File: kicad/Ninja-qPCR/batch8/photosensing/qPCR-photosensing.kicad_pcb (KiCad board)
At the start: 2 copper layers, 86.8 x 88 mm, 63 parts, among them J1 Conn_01x14_Male, J2 Conn_01x02_Male, J3 Conn_01x04_Male, J4 Conn_01x04_Male, U1 ADS122C04IPWR, U10 MCP4551T-503E/MS, U11 PCA9955B, U13 SN74LV4051APWR, U14 CD74HC4067M96, U15 TS12A12511DCNR, U2 ADA2200ARUZ, U3 LMP7717MF_NOPB, U4 COM1305-0.032768-EXT-T-TR, U5 TS12A12511DCNR, U6 CD74HC4067M96, U7 SN74LVC1GU04DCKR, U8 LM7705MMX_NOPB, U9 SN74LVC1GU04DCKR

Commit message: change footprints
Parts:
- moved LEDN1 1.85 mm to (95.0, 51.2)
- moved LEDS1 1.85 mm to (95.0, 100.8)
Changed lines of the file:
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@@
   )
   (module Pin_Headers:Pin_Header_Straight_1x10_Pitch2.54mm (layer F.Cu)
-    (at 95 49.3005 90)
+    (at 95 51.1505 90)
     (descr "Through hole straight pin header, 1x10, 2.54mm pitch, single row")
     (tags "Through hole pin header THT 1x10 2.54mm single row")
@@
   )
   (module Pin_Headers:Pin_Header_Straight_1x10_Pitch2.54mm (layer F.Cu)
-    (at 95 102.6995 90)
+    (at 95 100.8495 90)
     (descr "Through hole straight pin header, 1x10, 2.54mm pitch, single row")
     (tags "Through hole pin header THT 1x10 2.54mm single row")

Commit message: change footprints
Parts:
- moved JPDS1 3.14 mm to (107.0, 88.1)
- moved JPDN1 2.86 mm to (107.0, 65.1)

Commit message: Photosensing artwork
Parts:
- moved R7 92.2 mm to (94.8, 109.6)
- moved U10 90.3 mm to (87.6, 104.3), turned to 180 degrees
- moved U11 87.5 mm to (88.5, 112.0), turned to 270 degrees
- moved C17 80.0 mm to (56.3, 118.5)
- moved C16 77.8 mm to (56.6, 113.3)
- moved TLID1 76.3 mm to (112.5, 92.9)
- moved TWELL1 75.8 mm to (112.5, 97.0)
- moved C14 72.5 mm to (88.7, 67.8), turned to 90 degrees
- moved C15 71.8 mm to (90.7, 66.8), turned to 90 degrees
- moved C11 69.1 mm to (87.2, 67.8), turned to 90 degrees
- moved FB1 69.0 mm to (92.4, 67.7), turned to 90 degrees
- moved J2 66.3 mm to (91.1, 93.1), turned to 270 degrees
- moved U8 64.9 mm to (84.3, 64.1)
- moved C12 64.4 mm to (91.0, 62.5), turned to 180 degrees
- moved C13 61.4 mm to (90.0, 60.6), turned to 180 degrees
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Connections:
- U13 pad 2: (no net) -> Net-(U13-Pad2)
- U13 pad 4: (no net) -> Net-(U13-Pad4)
- U14 pad 16: /Sheet60C04E5B/N_PD_OUT16 -> /Sheet60C04E5B/N_PD_OUT2
- U14 pad 17: /Sheet60C04E5B/N_PD_OUT15 -> /Sheet60C04E5B/N_PD_OUT4
- U14 pad 18: /Sheet60C04E5B/N_PD_OUT14 -> /Sheet60C04E5B/N_PD_OUT6
- U14 pad 19: /Sheet60C04E5B/N_PD_OUT13 -> /Sheet60C04E5B/N_PD_OUT8
- U14 pad 2: /Sheet60C04E5B/N_PD_OUT8 -> /Sheet60C04E5B/N_PD_OUT15
- U14 pad 20: /Sheet60C04E5B/N_PD_OUT12 -> /Sheet60C04E5B/N_PD_OUT10
- U14 pad 21: /Sheet60C04E5B/N_PD_OUT11 -> /Sheet60C04E5B/N_PD_OUT12
- U14 pad 22: /Sheet60C04E5B/N_PD_OUT10 -> /Sheet60C04E5B/N_PD_OUT14
- U14 pad 23: /Sheet60C04E5B/N_PD_OUT9 -> /Sheet60C04E5B/N_PD_OUT16
- U14 pad 3: /Sheet60C04E5B/N_PD_OUT7 -> /Sheet60C04E5B/N_PD_OUT13
- U14 pad 4: /Sheet60C04E5B/N_PD_OUT6 -> /Sheet60C04E5B/N_PD_OUT11
- U14 pad 5: /Sheet60C04E5B/N_PD_OUT5 -> /Sheet60C04E5B/N_PD_OUT9
- U14 pad 6: /Sheet60C04E5B/N_PD_OUT4 -> /Sheet60C04E5B/N_PD_OUT7
- U14 pad 7: /Sheet60C04E5B/N_PD_OUT3 -> /Sheet60C04E5B/N_PD_OUT5
- U14 pad 8: /Sheet60C04E5B/N_PD_OUT2 -> /Sheet60C04E5B/N_PD_OUT3
- U15 pad 5: (no net) -> Net-(U15-Pad5)
- U2 pad 2: (no net) -> Net-(U2-Pad2)
- U5 pad 5: (no net) -> Net-(U5-Pad5)
- U6 pad 16: /Sheet60AF0517/S_PD_OUT16 -> /Sheet60AF0517/S_PD_OUT15
- U6 pad 17: /Sheet60AF0517/S_PD_OUT15 -> /Sheet60AF0517/S_PD_OUT13
- U6 pad 18: /Sheet60AF0517/S_PD_OUT14 -> /Sheet60AF0517/S_PD_OUT11
- U6 pad 19: /Sheet60AF0517/S_PD_OUT13 -> /Sheet60AF0517/S_PD_OUT9
- U6 pad 2: /Sheet60AF0517/S_PD_OUT8 -> /Sheet60AF0517/S_PD_OUT2
- U6 pad 20: /Sheet60AF0517/S_PD_OUT12 -> /Sheet60AF0517/S_PD_OUT7
- U6 pad 21: /Sheet60AF0517/S_PD_OUT11 -> /Sheet60AF0517/S_PD_OUT5
- U6 pad 22: /Sheet60AF0517/S_PD_OUT10 -> /Sheet60AF0517/S_PD_OUT3
- U6 pad 23: /Sheet60AF0517/S_PD_OUT9 -> /Sheet60AF0517/S_PD_OUT1
- U6 pad 3: /Sheet60AF0517/S_PD_OUT7 -> /Sheet60AF0517/S_PD_OUT4
- U6 pad 5: /Sheet60AF0517/S_PD_OUT5 -> /Sheet60AF0517/S_PD_OUT8
- U6 pad 6: /Sheet60AF0517/S_PD_OUT4 -> /Sheet60AF0517/S_PD_OUT10
- U6 pad 7: /Sheet60AF0517/S_PD_OUT3 -> /Sheet60AF0517/S_PD_OUT12
- U6 pad 8: /Sheet60AF0517/S_PD_OUT2 -> /Sheet60AF0517/S_PD_OUT14
- U6 pad 9: /Sheet60AF0517/S_PD_OUT1 -> /Sheet60AF0517/S_PD_OUT16
- U7 pad 1: (no net) -> Net-(U7-Pad1)
- U9 pad 1: (no net) -> Net-(U9-Pad1)
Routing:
- net MUX_S0: track 0.00 -> 216.1 mm, vias 0 -> 4
- net MUX_S1: track 0.00 -> 211.1 mm, vias 0 -> 6
- net MUX_SELECT: track 0.00 -> 200.7 mm, vias 0 -> 6
- net 3V3D: track 0.00 -> 198.9 mm, vias 0 -> 7
- net MUX_S3: track 0.00 -> 189.6 mm, vias 0 -> 7
- net MUX_S2: track 0.00 -> 188.3 mm, vias 0 -> 6
- net GNDD: track 86.5 -> 243.6 mm, vias 0 -> 2
- net GNDA: track 0.00 -> 123.5 mm, vias 0 -> 2
- net N_LED_OUT8: track 0.00 -> 110.6 mm, vias 0 -> 1
- net N_LED_OUT7: track 0.00 -> 109.7 mm, vias 0 -> 1
- net N_LED_OUT6: track 0.00 -> 106.4 mm, vias 0 -> 1
- net N_LED_OUT5: track 0.00 -> 104.9 mm, vias 0 -> 1
- net N_LED_OUT4: track 0.00 -> 103.4 mm, vias 0 -> 1
- net N_LED_OUT3: track 0.00 -> 100.3 mm, vias 0 -> 1
- net N_LED_OUT2: track 0.00 -> 97.0 mm, vias 0 -> 1
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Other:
- outline, holes or cut-outs redrawn
- board text removed: "ADA2200"
- board text removed: "Gain Sw"
- board text removed: "LED Driver"
- board text removed: "Neg.V"
- board text removed: "North PD MUX"
- board text removed: "OpAmp"
- board text removed: "POT"
- board text removed: "Photo N/S Inverter"
- board text removed: "South PD MUX"

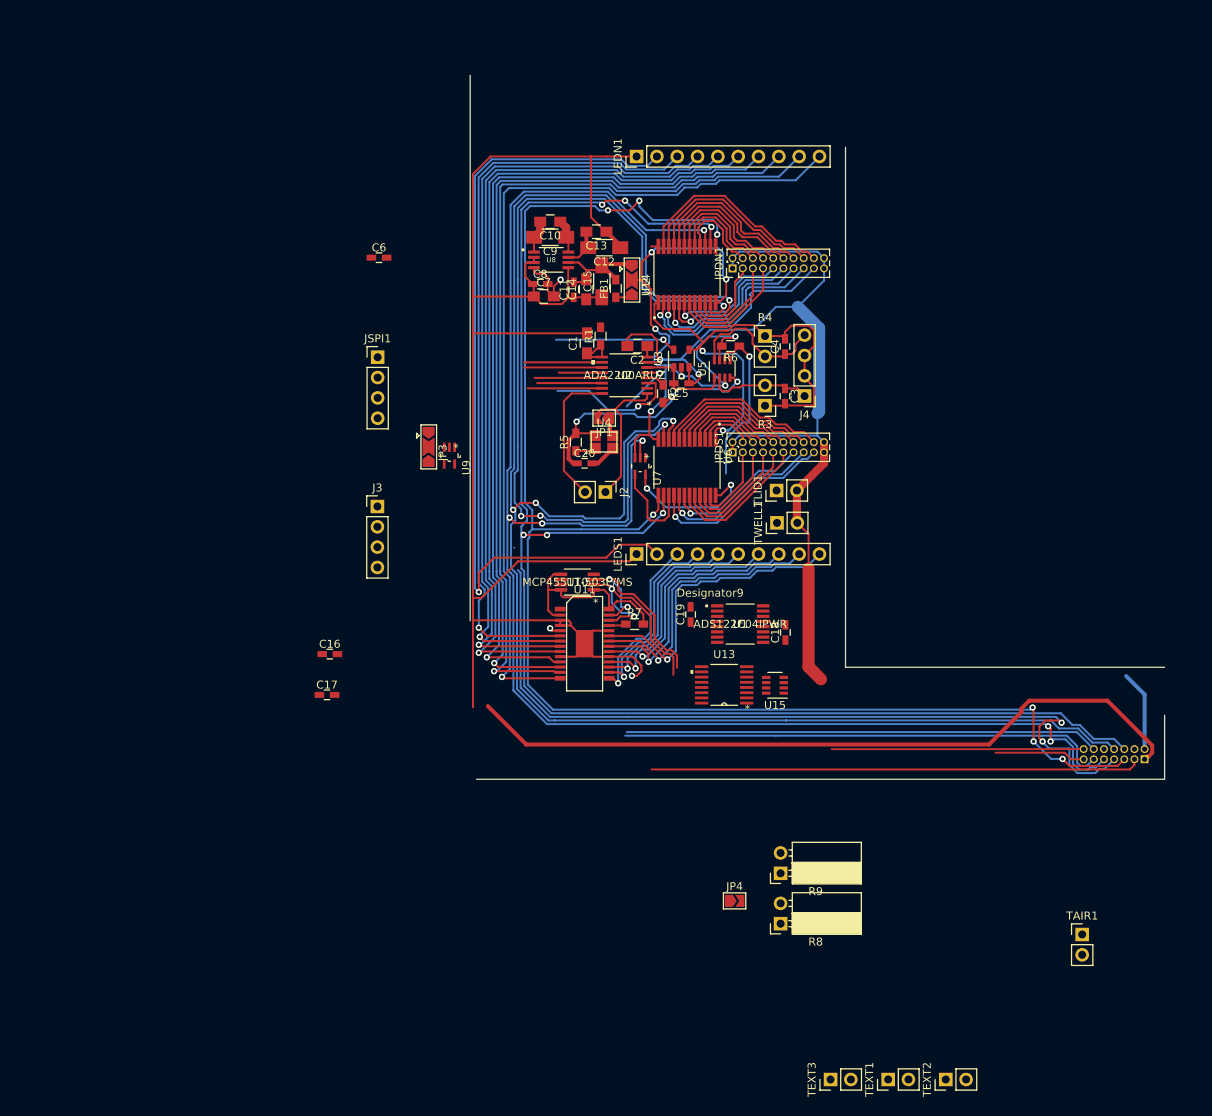
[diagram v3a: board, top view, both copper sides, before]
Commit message: Update photosensing board / replace thermistor connectors
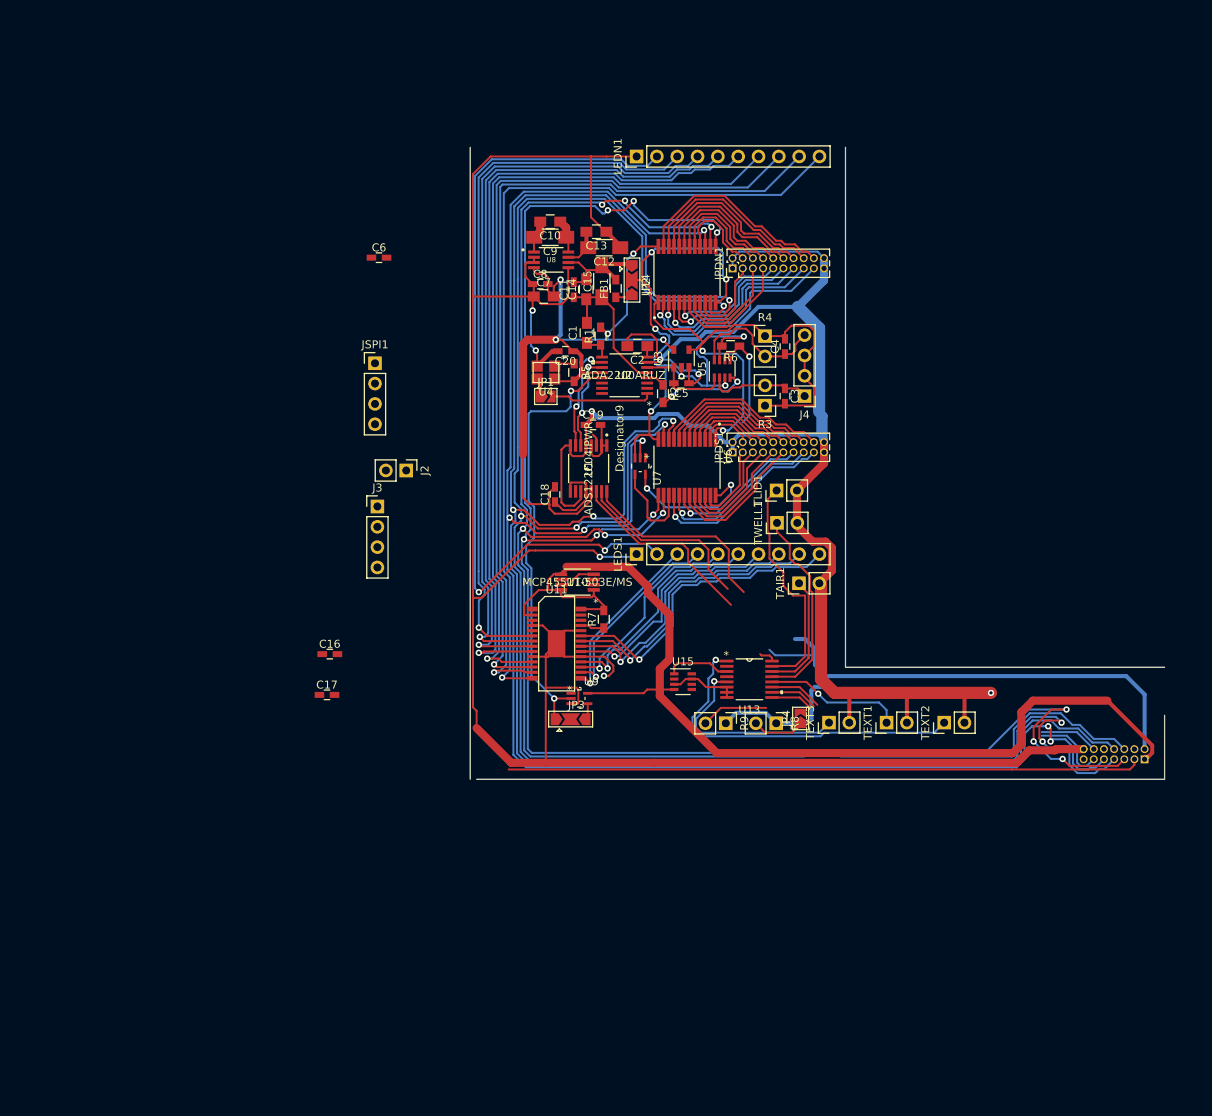
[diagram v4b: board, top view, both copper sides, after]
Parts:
- R8, R9: footprint Socket_Strips:Socket_Strip_Angled_1x02_Pitch2.54mm -> Pin_Headers:Pin_Header_Straight_1x02_Pitch2.54mm
- moved TAIR1 56.4 mm to (115.3, 104.5), turned to 90 degrees
- moved TEXT1 44.6 mm to (126.2, 121.9)
- moved TEXT2 44.6 mm to (133.4, 121.9)
- moved TEXT3 44.6 mm to (119.0, 121.9)
- moved JP3 38.4 mm to (86.8, 121.5), turned to 0 degrees
- moved U9 34.4 mm to (87.8, 118.9), turned to 0 degrees
- moved C18 33.6 mm to (84.8, 93.4)
- moved U1 27.2 mm to (89.0, 90.2), turned to 270 degrees
- moved C19 26.7 mm to (89.5, 84.7), turned to 0 degrees
- moved R8 25.1 mm to (112.5, 122.0), turned to 270 degrees
- moved J2 25.0 mm to (66.2, 90.4)
- moved JP4 24.2 mm to (115.5, 121.4), turned to 90 degrees
- moved R9 20.0 mm to (106.2, 122.0), turned to 270 degrees
- moved C20 14.2 mm to (86.1, 75.5), turned to 180 degrees
- moved U15 11.5 mm to (100.8, 116.8), turned to 0 degrees
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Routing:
- net GNDD: track 243.6 -> 327.2 mm, vias 2 -> 4
- net GNDA: track 123.5 -> 203.4 mm, vias 2 -> 4
- net 3V3A: track 10.1 -> 89.1 mm
- net 3V3D: track 198.9 -> 265.7 mm, vias 7 -> 9
- net I2C_SDA: track 85.1 -> 30.4 mm, vias 2 -> 0
- net I2C_SCL: track 87.9 -> 34.7 mm, vias 2 -> 0
- net PD_REF_PWM: track 8.46 -> 54.9 mm, vias 0 -> 2
- net THERM_EXT2: track 0.00 -> 43.9 mm, vias 0 -> 1
- net THERM_LID: track 0.00 -> 28.7 mm
- net THERM_EXT3: track 0.00 -> 25.9 mm, vias 0 -> 1
- net THERM_WELL: track 0.00 -> 25.2 mm
- net ADC_DRDY: track 0.00 -> 24.3 mm
- net MUX_S1: track 211.1 -> 232.1 mm
- net MUX_S3: track 189.6 -> 208.1 mm, vias 7 -> 9
- net XOUT: track 17.6 -> 0.00 mm
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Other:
- board size 86.8 x 88 mm -> 86.8 x 79 mm
- board text removed: "ADC"
- board text removed: "Ext Xtal"
- board text removed: "RCLK Inv"
- board text removed: "SPI Debug"

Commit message: minor changes
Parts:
- J1: value Conn_01x14_Male -> Conn_01x20_Male; footprint Pin_Headers:Pin_Header_Straight_2x07_Pitch1.27mm -> Pin_Headers:Pin_Header_Straight_2x10_Pitch1.27mm; moved to F.Cu
- moved J1 3.83 mm to (162.1, 125.2), turned to 270 degrees
- moved C1 0.20 mm to (88.6, 73.2)
- moved C10 0.20 mm to (84.0, 59.3)
- moved C11 0.20 mm to (87.0, 67.8)
- moved C12 0.20 mm to (90.8, 62.5)
- moved C13 0.20 mm to (89.8, 60.6)
- moved C14 0.20 mm to (88.5, 67.8)
- moved C15 0.20 mm to (90.5, 66.8)
- moved C18 0.20 mm to (84.6, 93.4)
- moved C19 0.20 mm to (89.3, 84.7)
- moved C3 0.20 mm to (113.3, 81.1)
- moved C4 0.20 mm to (113.3, 74.9)
- moved C7 0.20 mm to (83.2, 68.7)
- moved C8 0.20 mm to (82.8, 67.1)
- moved C9 0.20 mm to (84.0, 61.2)
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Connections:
- J1 pad 1: 3V3D -> (no net)
- J1 pad 10: ADC_DRDY -> VCC_LED
- J1 pad 11: I2C_SCL -> MUX_S2
- J1 pad 12: I2C_SDA -> MUX_S3
- J1 pad 13: THERM_R_SWITCH -> MUX_S0
- J1 pad 14: GNDD -> MUX_S1
- J1 pad 2: 3V3A -> (no net)
- J1 pad 3: VCC_LED -> (no net)
- J1 pad 4: AMP_GAIN_SW -> (no net)
- J1 pad 5: MUX_S3 -> (no net)
- J1 pad 6: MUX_S2 -> (no net)
- J1 pad 7: MUX_S1 -> 3V3A
- J1 pad 8: MUX_S0 -> 3V3D
- J1 pad 9: MUX_SELECT -> AMP_GAIN_SW
- U13 pad 2: Net-(U13-Pad2) -> (no net)
- U13 pad 4: Net-(U13-Pad4) -> (no net)
- U15 pad 5: Net-(U15-Pad5) -> (no net)
- U2 pad 2: Net-(U2-Pad2) -> (no net)
- U5 pad 5: Net-(U5-Pad5) -> (no net)
- U7 pad 1: Net-(U7-Pad1) -> (no net)
- U9 pad 1: Net-(U9-Pad1) -> (no net)
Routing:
- net 3V3D: track 265.7 -> 264.0 mm
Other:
- board size 86.8 x 79 mm -> 89.5 x 80.5 mm

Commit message: Photosensing artwork
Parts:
- removed the J1 at (162.1, 125.2)
- removed J2: Conn_01x02_Male, Pin_Headers:Pin_Header_Straight_1x02_Pitch2.54mm
- added J1: Conn_01x14_Male, Pin_Headers:Pin_Header_Straight_2x07_Pitch1.27mm, B.Cu at (158.5, 126.5)
- added J1: Conn_01x20_Male, Pin_Headers:Pin_Header_Straight_2x10_Pitch1.27mm, F.Cu at (158.4, 130.8)
- moved JSPI1 52.6 mm to (110.2, 55.8), turned to 90 degrees
- moved C16 37.2 mm to (92.6, 122.2), turned to 180 degrees
- moved TEXT2 30.9 mm to (105.2, 109.0), turned to 180 degrees
- moved J3 23.3 mm to (83.2, 84.5)
- moved C6 22.3 mm to (83.5, 71.6), turned to 90 degrees
- moved TEXT1 21.2 mm to (109.2, 109.0), turned to 180 degrees
- moved C17 20.7 mm to (76.6, 121.0), turned to 270 degrees
- moved TEXT3 11.9 mm to (114.2, 111.0), turned to 180 degrees
- moved U10 3.22 mm to (84.2, 104.8)
- moved C19 2.41 mm to (91.8, 84.9)
- moved C18 2.41 mm to (87.0, 93.6)
- moved U1 2.41 mm to (91.2, 90.3)
- moved JP1 1.65 mm to (81.8, 81.3)
- moved C10 1.32 mm to (84.2, 58.0)
- moved C9 1.07 mm to (84.2, 60.2)
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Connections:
- U13 pad 2: (no net) -> Net-(U13-Pad2)
- U13 pad 4: (no net) -> Net-(U13-Pad4)
- U15 pad 5: (no net) -> Net-(U15-Pad5)
- U2 pad 2: (no net) -> Net-(U2-Pad2)
- U5 pad 5: (no net) -> Net-(U5-Pad5)
- U7 pad 1: (no net) -> Net-(U7-Pad1)
- U9 pad 1: (no net) -> Net-(U9-Pad1)
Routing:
- net AMP_GAIN_SW: track 13.4 -> 108.6 mm
- net DEMOD_SPI_CS: track 0.00 -> 77.3 mm, vias 0 -> 2
- net DEMOD_SPI_SDIO: track 0.00 -> 69.2 mm, vias 0 -> 2
- net I2C_SDA: track 30.4 -> 97.4 mm, vias 0 -> 4
- net DEMOD_SPI_SCLK: track 0.00 -> 64.4 mm, vias 0 -> 2
- net ADC_DRDY: track 24.3 -> 86.3 mm, vias 0 -> 2
- net I2C_SCL: track 34.7 -> 96.5 mm, vias 0 -> 4
- net 3V3D: track 264.0 -> 324.9 mm, vias 9 -> 15
- net GNDD: track 327.2 -> 386.5 mm, vias 4 -> 6
- net THERM_MUX_OUT: track 8.09 -> 58.3 mm, vias 0 -> 4
- net THERM_R_SWITCH: track 0.00 -> 40.2 mm, vias 0 -> 2
- net THERM_EXT2: track 43.9 -> 7.42 mm
- net PD_MUX_OUT: track 64.7 -> 95.9 mm
- net 3V3A: track 89.1 -> 118.4 mm
- net /AMP_OUT: track 12.2 -> 38.6 mm, vias 0 -> 1
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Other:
- board size 89.5 x 80.5 mm -> 86.8 x 79 mm
- board text removed: "Demod Debug"

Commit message: Photosensing artwork
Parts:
- removed the J1 at (158.5, 126.5)
- moved J1 5.60 mm to (158.4, 125.2)
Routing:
- net MUX_S3: track 208.7 -> 194.5 mm, vias 9 -> 7
- net MUX_S1: track 241.7 -> 227.7 mm, vias 7 -> 5
- net GNDA: track 205.5 -> 192.1 mm, vias 6 -> 5
- net MUX_SELECT: track 211.5 -> 199.8 mm, vias 6 -> 5
- net I2C_SCL: track 96.5 -> 108.0 mm
- net THERM_R_SWITCH: track 40.2 -> 50.8 mm, vias 2 -> 1
- net 3V3A: track 118.4 -> 110.9 mm, vias 0 -> 1
- net ADC_DRDY: track 86.3 -> 79.7 mm
- net I2C_SDA: track 97.4 -> 101.8 mm
- net MUX_S0: track 238.3 -> 234.1 mm, vias 5 -> 6
- net MUX_S2: track 208.0 -> 203.9 mm, vias 7 -> 8
- net 3V3D: track 324.9 -> 328.3 mm
- net DEMOD_SPI_SDIO: track 69.2 -> 65.9 mm
- net GNDD: track 386.5 -> 383.7 mm, vias 6 -> 7
- net N_LED_OUT7: track 106.2 -> 103.5 mm
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
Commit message: cleanup
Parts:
- moved C17 2.09 mm to (76.0, 119.0)
- moved J1 0.20 mm to (158.2, 125.2)
- moved C1 0.20 mm to (88.6, 73.2)
- moved C10 0.20 mm to (84.0, 58.0)
- moved C11 0.20 mm to (87.0, 67.8)
- moved C12 0.20 mm to (90.8, 62.5)
- moved C13 0.20 mm to (89.8, 60.6)
- moved C14 0.20 mm to (88.5, 67.8)
- moved C15 0.20 mm to (90.5, 66.8)
- moved C18 0.20 mm to (86.8, 93.6)
- moved C19 0.20 mm to (91.5, 84.9)
- moved C3 0.20 mm to (113.3, 80.5)
- moved C4 0.20 mm to (113.3, 74.3)
- moved C6 0.20 mm to (83.3, 71.6)
- moved C7 0.20 mm to (83.2, 68.7)
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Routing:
- net GNDA: track 192.1 -> 167.1 mm
- net GNDD: track 383.7 -> 367.8 mm
- net 3V3A: track 110.9 -> 108.1 mm
- net AMP_GAIN_SW: track 106.8 -> 108.7 mm
- net VCC_LED: track 202.9 -> 202.0 mm
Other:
- board size 86.8 x 79 mm -> 86.5 x 79.5 mm
